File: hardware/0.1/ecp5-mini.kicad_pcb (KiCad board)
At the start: 4 copper layers, 52 x 27 mm, 105 parts, among them J1 Micro_SD_Card, J2 JTAG, J3 S7 Mini, J4 S7 Mini, J5 USB_C_Receptacle_USB2.0, Q1 BSS138, Q2 BSS138, Q3 BSS138, Q4 BSS138, SW1 SW_Push, U1 ECP5U_12_CABGA256, U2 TLV73325PDBV, U3 TLV62568DBV, U4 USBLC6-2SC6, U5 TLV62568DBV, U6 W25Q128JVSIQ, U7 S27KL0641, X1 DSC6101CI2A-016

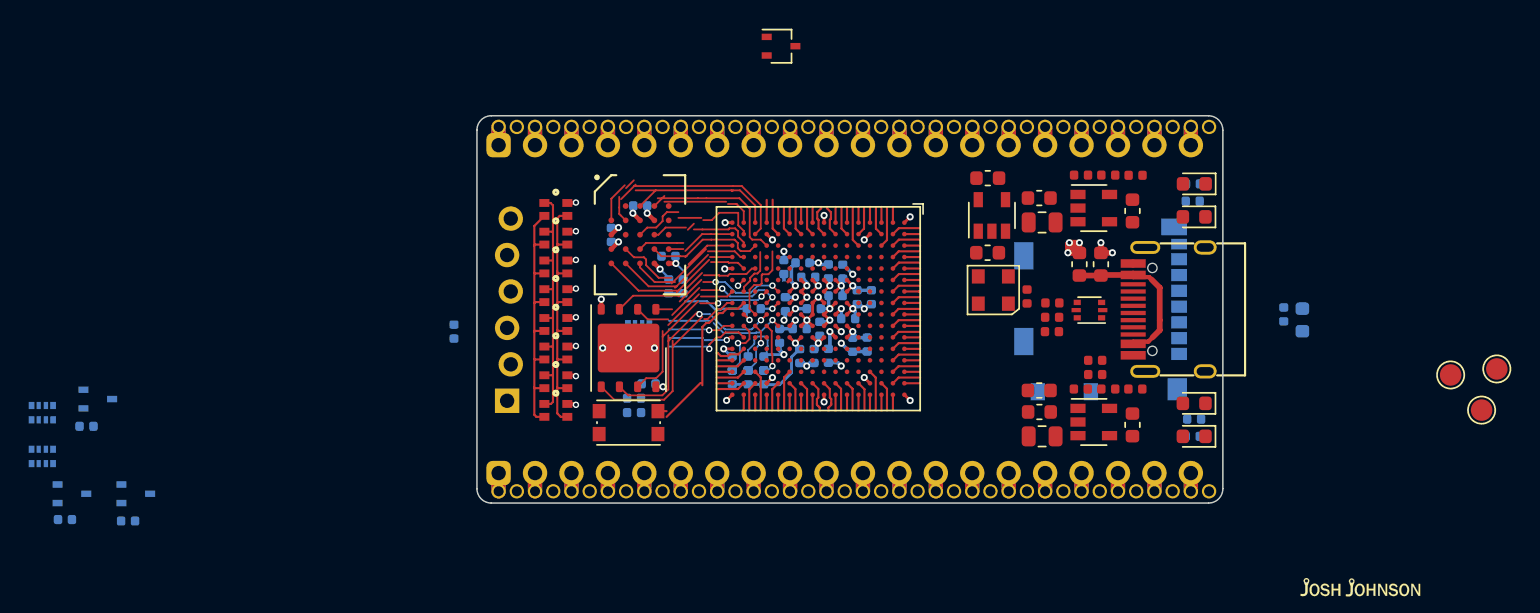
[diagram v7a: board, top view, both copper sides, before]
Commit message: hyperram routed
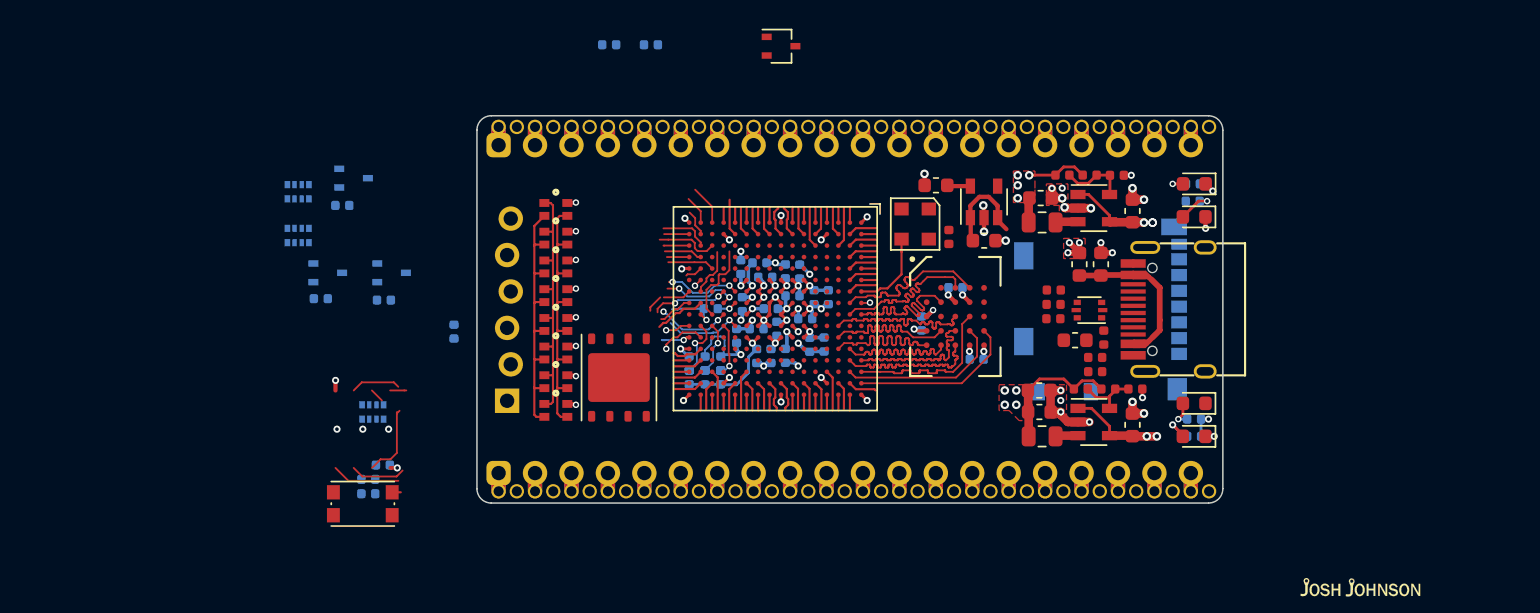
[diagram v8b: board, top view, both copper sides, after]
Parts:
- removed TP1: 2v5, TestPoint:TestPoint_Pad_D1.5mm
- removed TP2: 3V3, TestPoint:TestPoint_Pad_D1.5mm
- removed TP3: 1v1, TestPoint:TestPoint_Pad_D1.5mm
- C11, C12: moved to F.Cu
- moved R30 23.6 mm to (89.7, 94.3)
- moved Q3 23.6 mm to (87.6, 85.8)
- moved RN2 23.6 mm to (83.7, 86.8)
- moved RN3 23.6 mm to (83.7, 89.8)
- moved Q2 23.6 mm to (85.8, 92.4)
- moved Q4 23.6 mm to (90.2, 92.4)
- moved R25 23.6 mm to (85.3, 94.2)
- moved R28 23.6 mm to (86.8, 87.7)
- moved U7 22.7 mm to (129.6, 95.4)
- moved C46 22.7 mm to (129.6, 93.4)
- moved C45 22.7 mm to (131.0, 98.4)
- moved C47 22.5 mm to (127.2, 95.9)
- moved RN1 19.4 mm to (88.9, 102.1)
- moved SW1 19.4 mm to (88.2, 108.5)
- moved C13 19.4 mm to (88.6, 106.8)
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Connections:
- U1 pad A13: Net-(U1-PadA13) -> /HR_DQ0
- U1 pad A14: Net-(U1-PadA14) -> /HR_DQ2
- U1 pad A15: Net-(U1-PadA15) -> /HR_DQ4
- U1 pad A9: Net-(U1-PadA9) -> /HR_CK
- U1 pad B12: Net-(U1-PadB12) -> /HR_DQ6
- U1 pad B13: Net-(U1-PadB13) -> /HR_DQ5
- U1 pad B14: Net-(U1-PadB14) -> /HR_DQ3
- U1 pad B8: Net-(U1-PadB8) -> /HR_nRST
- U1 pad B9: Net-(U1-PadB9) -> /HR_nCS
- U1 pad C10: Net-(U1-PadC10) -> /HR_RWDS
- U1 pad C11: Net-(U1-PadC11) -> /HR_DQ1
- U1 pad C12: Net-(U1-PadC12) -> /HR_DQ7
- U1 pad N3: /HR_nCS -> Net-(U1-PadN3)
- U1 pad P1: /HR_CK_P -> Net-(U1-PadP1)
- U1 pad P2: /HR_CK_N -> Net-(U1-PadP2)
- U1 pad P3: /HR_DQ4 -> Net-(U1-PadP3)
- U1 pad P5: /HR_DQ7 -> Net-(U1-PadP5)
- U1 pad R1: /HR_nRST -> Net-(U1-PadR1)
- U1 pad R2: /HR_RWDS -> Net-(U1-PadR2)
- U1 pad R3: /HR_DQ2 -> Net-(U1-PadR3)
- U1 pad R4: /HR_DQ1 -> Net-(U1-PadR4)
- U1 pad R5: /HR_DQ6 -> Net-(U1-PadR5)
- U1 pad T2: /HR_DQ0 -> Net-(U1-PadT2)
- U1 pad T3: /HR_DQ3 -> Net-(U1-PadT3)
- U1 pad T4: /HR_DQ5 -> Net-(U1-PadT4)
- U7 pad B1: /HR_CK_N -> Net-(U7-PadB1)
- U7 pad B2: /HR_CK_P -> /HR_CK
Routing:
- net +5V: track 42.0 -> 65.8 mm, vias 3 -> 8
- net GND: track 43.7 -> 62.7 mm, vias 38 -> 60
- net /HR_CK_N: track 16.6 -> 0.00 mm
- net /HR_CK: track 0.00 -> 12.0 mm
- net /HR_CK_P: track 11.8 -> 0.00 mm
- net +1V1: track 11.7 -> 21.1 mm, vias 5 -> 9
- net +3V3: track 23.4 -> 31.8 mm, vias 11 -> 16
- net /FPGA Config/nBTN_USR: track 11.6 -> 4.18 mm
- net /FPGA Config/CFG.IO0: track 14.5 -> 7.19 mm
- net /FPGA Config/CFG.CLK: track 16.0 -> 8.98 mm
- net /FPGA Config/CFG.IO2: track 15.0 -> 8.79 mm
- net /HR_DQ3: track 6.05 -> 11.6 mm
- net Net-(C6-Pad1): track 13.5 -> 18.7 mm
- net /CLK_16MHZ: track 1.10 -> 5.79 mm
- net Net-(C9-Pad2): track 0.00 -> 4.68 mm
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- added copper zone on F.Cu, net +1V1
- added copper zone on F.Cu, net +3V3
- added copper zone on F.Cu, net +5V
- added copper zone on In2.Cu, net +5V
- added copper zone on F.Cu, net GND
